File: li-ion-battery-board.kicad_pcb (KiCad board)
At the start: 2 copper layers, 101.6 x 6.4 mm, 11 parts, among them J1 Conn_01x02_Female, Q1 MOSFET, Q2 MOSFET, SW1 SW_SP3T, U1 AP9101CK6

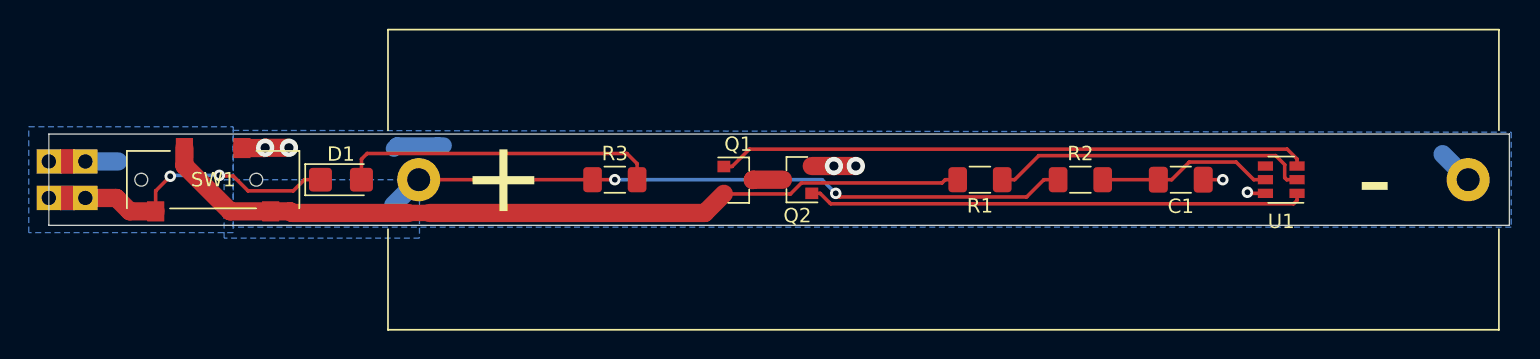
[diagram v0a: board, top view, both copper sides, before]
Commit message: Add mounting holes and modify silkscreen text.
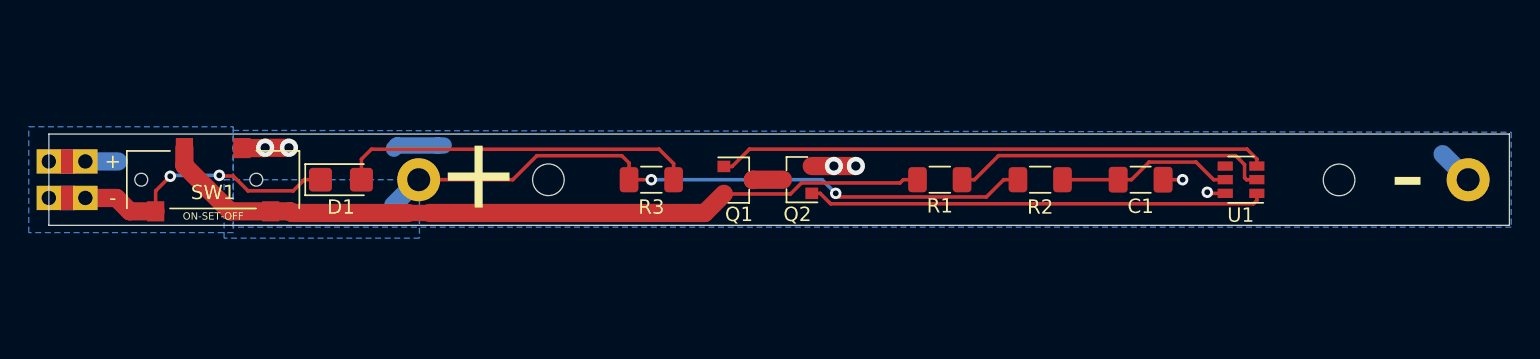
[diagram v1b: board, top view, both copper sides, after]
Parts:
- added M1: MountingHole_2.2mm_M2, MountingHole:MountingHole_2.2mm_M2, F.Cu at (191.3, 104.8)
- added M1: MountingHole_2.2mm_M2, MountingHole:MountingHole_2.2mm_M2, F.Cu at (136.3, 104.8)
- moved C1 2.79 mm to (177.5, 104.8)
- moved R1 2.79 mm to (163.6, 104.8)
- moved R2 2.79 mm to (170.6, 104.8)
- moved U1 2.79 mm to (184.5, 104.8)
- moved R3 2.54 mm to (143.5, 104.8)
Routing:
- net Net-(Q1-Pad1): track 41.1 -> 38.3 mm
- net Net-(Q2-Pad1): track 34.6 -> 31.8 mm
- net SWITCH: track 57.3 -> 54.5 mm
- net Net-(D1-Pad2): track 22.2 -> 25.0 mm
- net +BATT: track 50.3 -> 49.5 mm
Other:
- board text added: "+"
- board text added: "-"
- board text added: "Li-Ion Battery Board Rev1-0 Alexander Fraser 16 August 2021"
- board text added: "ON-SET-OFF"
